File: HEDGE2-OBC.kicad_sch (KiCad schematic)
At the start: 36 parts, among them J1 SMA-J-P-X-RA-TH1, U1 ADP7158ARDZ-3.3-R7, U3 TXS0102QDCURQ1

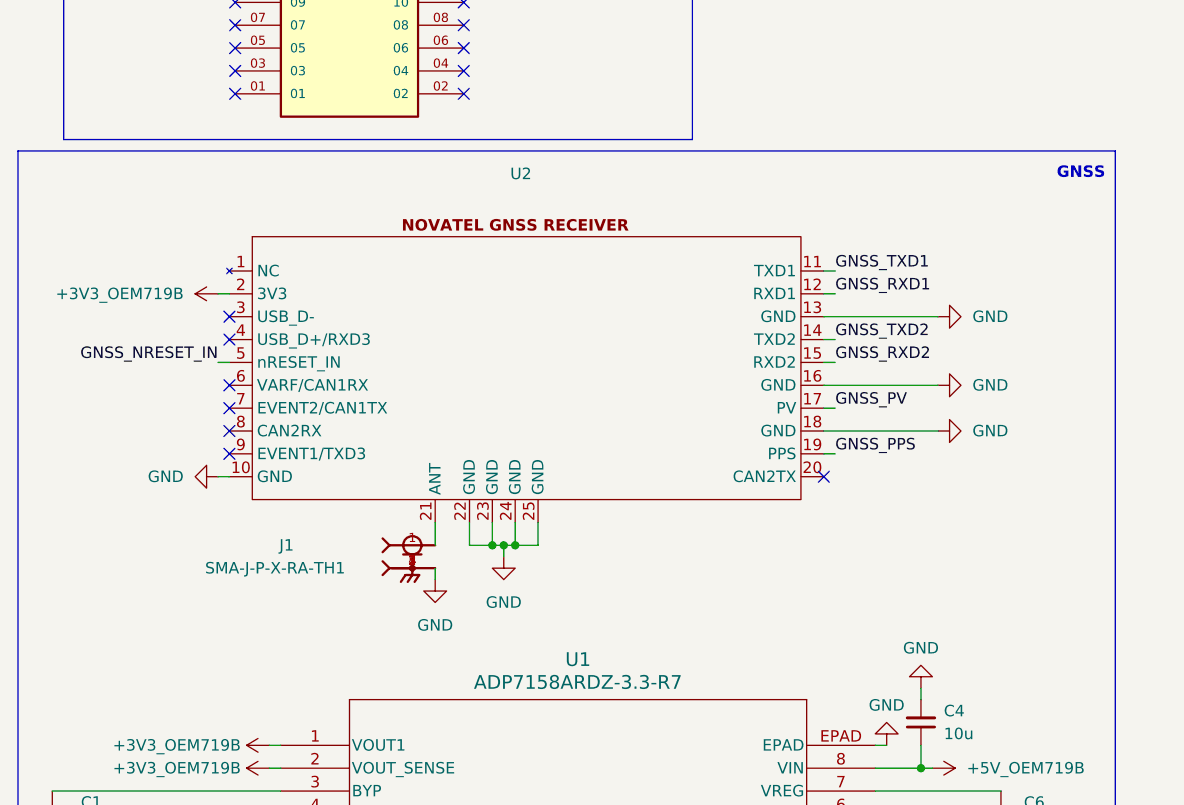
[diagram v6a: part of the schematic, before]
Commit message: Online DFM satisfactory
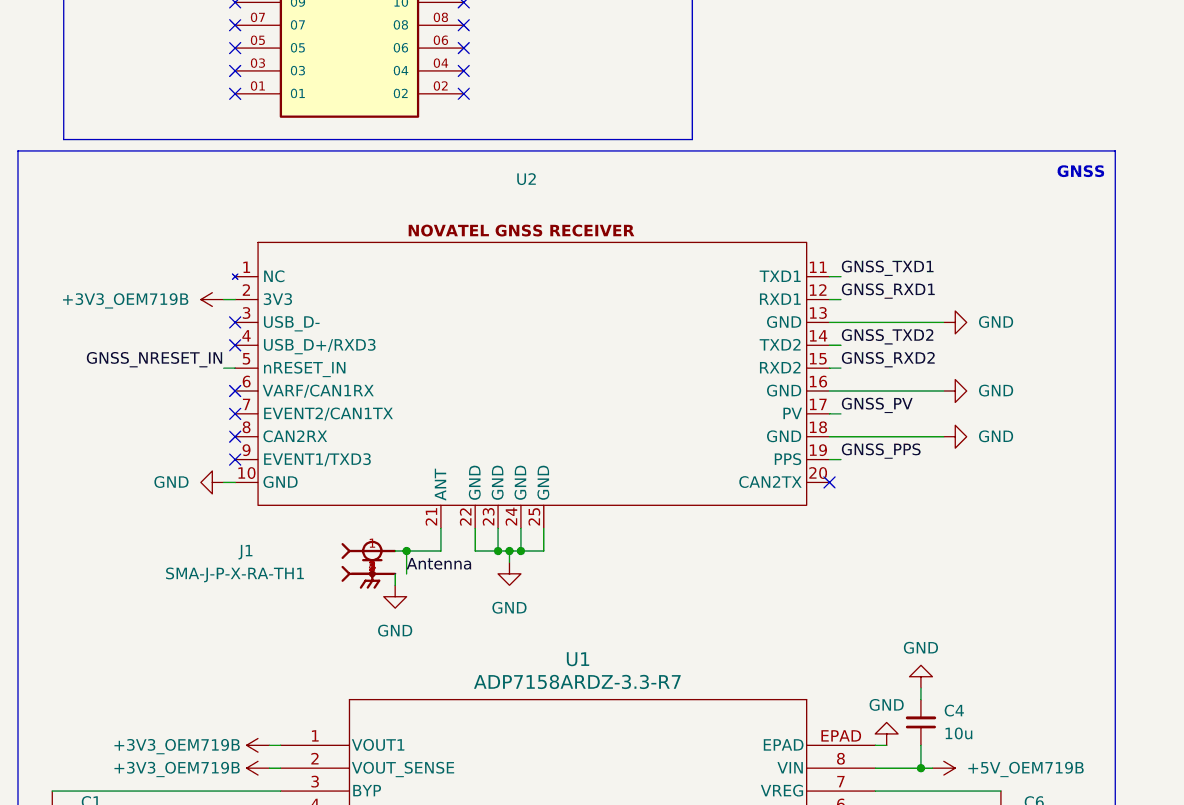
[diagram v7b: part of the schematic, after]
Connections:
- net Antenna: now reaches J1.1, U2.21 (ANT)
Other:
- moved on the sheet: J1, U2

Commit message: Verify CM4 and OEM710B footprints and clearances; add mounting hardware
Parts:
- Module1: DigiKey Part Number (none) -> 26-DF40HC(3.0)-100DS-0.4V(51)CT-ND
- Module1: DigiKey Part Number H11615CT-ND -> 26-DF40HC(3.0)-100DS-0.4V(51)CT-ND
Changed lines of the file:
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@@
+			)
+		)
+		(property "DigiKey Part Number" "26-DF40HC(3.0)-100DS-0.4V(51)CT-ND"
+			(at 280.67 83.82 0)
+			(effects
+				(font
+					(size 1.27 1.27)
+				)
+				(hide yes)
 			)
 		)
@@
 			)
 		)
-		(property "DigiKey Part Number" "H11615CT-ND"
+		(property "DigiKey Part Number" "26-DF40HC(3.0)-100DS-0.4V(51)CT-ND"
 			(at 241.3 88.9 0)
 			(effects
